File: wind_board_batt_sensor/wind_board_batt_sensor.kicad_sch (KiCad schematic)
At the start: 39 parts, among them J1 Batt +, J2 Batt -, J3 Sys +, J4 Sys -, J5 Conn_01x03_Socket, J6 Conn_01x02_Socket, U1 MAX17263xxTE, U3 ATtiny402-SS, U4 MCP16331x-xCH

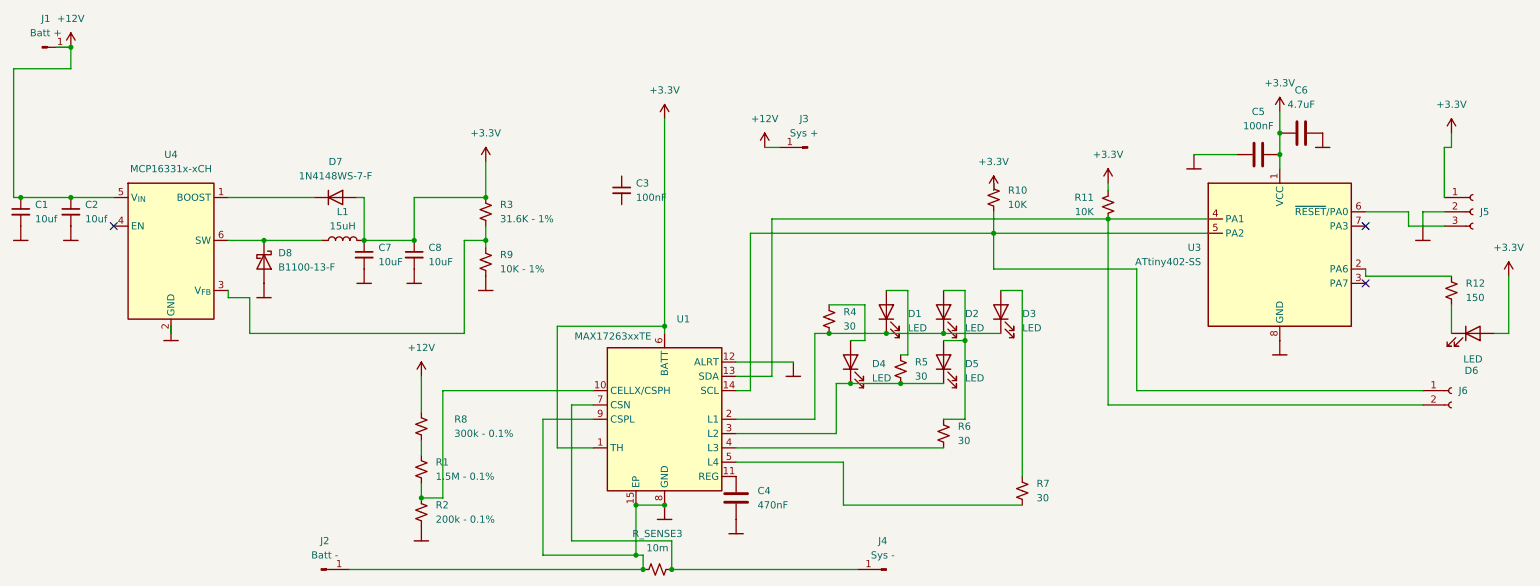
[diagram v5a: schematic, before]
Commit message: add new power supply
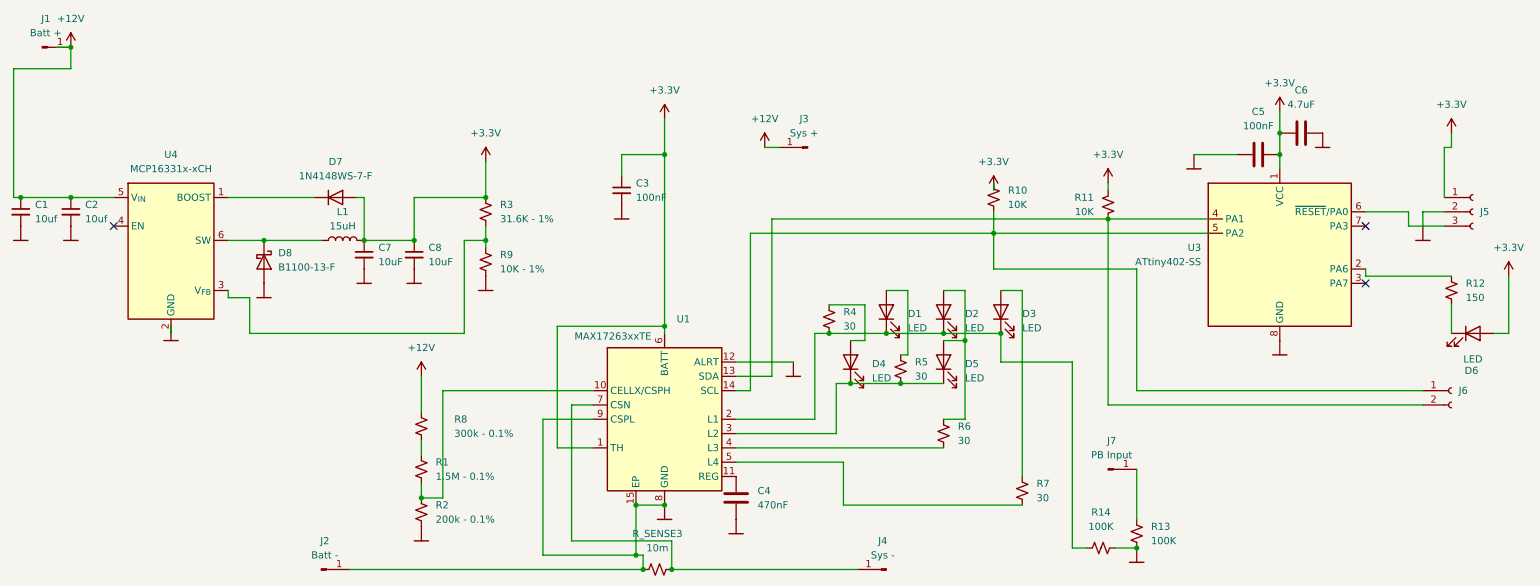
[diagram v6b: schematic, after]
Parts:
- added J7: PB Input, MountingHole:MountingHole_4.3mm_M4_ISO7380_Pad_TopBottom, symbol Connector:Conn_01x01_Pin
- added R13, R14: 100K, Resistor_SMD:R_0402_1005Metric, symbol Device:R_Small_US
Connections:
- net +3.3V: now also C3.1
- net at D1.1 (K), D2.1 (K), D3.1 (K)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: now also R14.1
- new net: R13.2, R14.2
- new net: J7.1 (Pin_1), R13.1

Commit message: new regulator
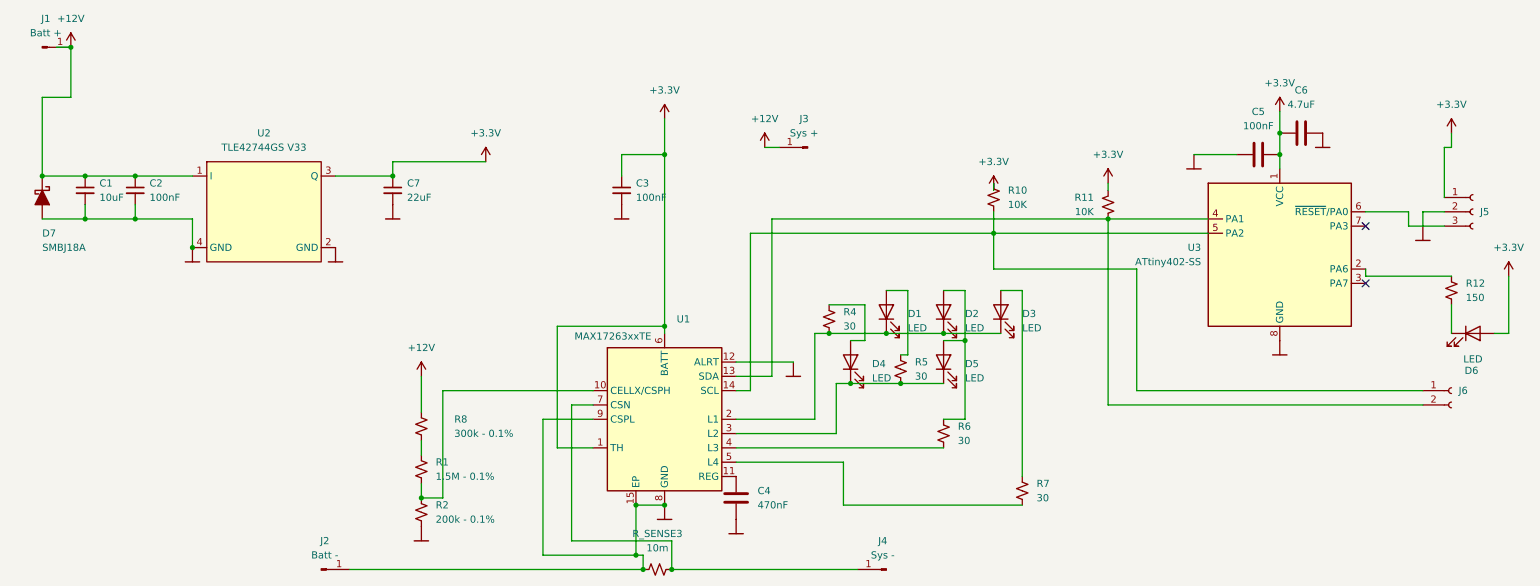
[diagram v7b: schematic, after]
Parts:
- removed C8: 10uF, Capacitor_SMD:C_0805_2012Metric, symbol Device:C_Small
- removed D7: 1N4148WS-7-F, Diode_SMD:D_SOD-323, symbol Device:D
- removed D8: B1100-13-F, Diode_SMD:D_SMA, symbol Device:D_Schottky
- removed J7: PB Input, MountingHole:MountingHole_4.3mm_M4_ISO7380_Pad_TopBottom, symbol Connector:Conn_01x01_Pin
- removed L1: 15uH, Inductor_SMD:L_7.3x7.3_H4.5, symbol Device:L
- removed R13, R14: 100K, Resistor_SMD:R_0402_1005Metric, symbol Device:R_Small_US
- removed R3: 31.6K - 1%, Resistor_SMD:R_0805_2012Metric, symbol Device:R_Small_US
- removed R9: 10K - 1%, Resistor_SMD:R_0805_2012Metric, symbol Device:R_Small_US
- removed U4: MCP16331x-xCH, Package_TO_SOT_SMD:SOT-23-6, symbol Regulator_Switching:MCP16331x-xCH
- added D7: SMBJ18A, Diode_SMD:D_SMB, symbol Device:D_Schottky_Filled
- added U2: TLE42744GS V33, Package_TO_SOT_SMD:SOT-223, symbol Regulator_Linear:TLE42744GSV33_1
- C1: value 10uf -> 10uF; footprint Capacitor_SMD:C_1210_3225Metric -> Capacitor_SMD:C_0805_2012Metric
- C2: value 10uf -> 100nF; footprint Capacitor_SMD:C_1210_3225Metric -> Capacitor_SMD:C_0805_2012Metric
- C7: value 10uF -> 22uF
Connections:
- net +12V: now also D7.1 (K), U2.1 (I)
- net +3.3V: now also U2.3 (Q)
- net at C2.2: now also C1.2, D7.2 (A), U2.4 (GND)
- no-connect marks 3 -> 2

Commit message: new power supply
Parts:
- C4, C6, R1, R10, R11, R2, R4, R5, R6, R7, R8: footprint Resistor_SMD:R_0805_2012Metric_Pad1.20x1.40mm_HandSolder -> Resistor_SMD:R_0805_2012Metric
- C5: footprint Resistor_SMD:R_0805_2012Metric_Pad1.20x1.40mm_HandSolder -> Capacitor_SMD:C_0805_2012Metric
- R_SENSE3: footprint Resistor_SMD:R_1206_3216Metric_Pad1.30x1.75mm_HandSolder -> Resistor_SMD:R_1206_3216Metric
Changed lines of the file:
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@@
 			)
 		)
-		(property "Footprint" "Resistor_SMD:R_1206_3216Metric_Pad1.30x1.75mm_HandSolder"
+		(property "Footprint" "Resistor_SMD:R_1206_3216Metric"
 			(at 128.27 113.03 0)
 			(effects
@@
 			)
 		)
-		(property "Footprint" "Resistor_SMD:R_0805_2012Metric_Pad1.20x1.40mm_HandSolder"
+		(property "Footprint" "Resistor_SMD:R_0805_2012Metric"
 			(at 246.38 34.5948 0)
 			(effects
@@
 			)
 		)
-		(property "Footprint" "Resistor_SMD:R_0805_2012Metric_Pad1.20x1.40mm_HandSolder"
+		(property "Footprint" "Resistor_SMD:R_0805_2012Metric"
 			(at 86.36 95.25 0)
 			(effects
@@
 			)
 		)
-		(property "Footprint" "Resistor_SMD:R_0805_2012Metric_Pad1.20x1.40mm_HandSolder"
+		(property "Footprint" "Resistor_SMD:R_0805_2012Metric"
 			(at 86.36 87.63 0)
 			(effects
@@
 			)
 		)
-		(property "Footprint" "Resistor_SMD:R_0805_2012Metric_Pad1.20x1.40mm_HandSolder"
+		(property "Footprint" "Capacitor_SMD:C_0805_2012Metric"
 			(at 238.76 38.4048 0)
 			(effects
@@
 			)
 		)
-		(property "Footprint" "Resistor_SMD:R_0805_2012Metric_Pad1.20x1.40mm_HandSolder"
+		(property "Footprint" "Resistor_SMD:R_0805_2012Metric"
 			(at 187.96 46.99 0)
 			(effects
@@
 			)
 		)
-		(property "Footprint" "Resistor_SMD:R_0805_2012Metric_Pad1.20x1.40mm_HandSolder"
+		(property "Footprint" "Resistor_SMD:R_0805_2012Metric"
 			(at 143.2052 104.14 0)
 			(effects
@@
 			)
 		)
-		(property "Footprint" "Resistor_SMD:R_0805_2012Metric_Pad1.20x1.40mm_HandSolder"
+		(property "Footprint" "Resistor_SMD:R_0805_2012Metric"
 			(at 86.36 102.87 0)
 			(effects
@@
 			)
 		)
-		(property "Footprint" "Resistor_SMD:R_0805_2012Metric_Pad1.20x1.40mm_HandSolder"
+		(property "Footprint" "Resistor_SMD:R_0805_2012Metric"
 			(at 158.75 68.58 0)
 			(effects
@@
 			)
 		)
-		(property "Footprint" "Resistor_SMD:R_0805_2012Metric_Pad1.20x1.40mm_HandSolder"
+		(property "Footprint" "Resistor_SMD:R_0805_2012Metric"
 			(at 171.45 77.47 0)
 			(effects
@@
 			)
 		)
-		(property "Footprint" "Resistor_SMD:R_0805_2012Metric_Pad1.20x1.40mm_HandSolder"
+		(property "Footprint" "Resistor_SMD:R_0805_2012Metric"
 			(at 179.07 88.9 0)
 			(effects
@@
 			)
 		)
-		(property "Footprint" "Resistor_SMD:R_0805_2012Metric_Pad1.20x1.40mm_HandSolder"
+		(property "Footprint" "Resistor_SMD:R_0805_2012Metric"
 			(at 208.28 48.26 0)
 			(effects
@@
 			)
 		)
-		(property "Footprint" "Resistor_SMD:R_0805_2012Metric_Pad1.20x1.40mm_HandSolder"
+		(property "Footprint" "Resistor_SMD:R_0805_2012Metric"
 			(at 193.04 99.06 0)
 			(effects
